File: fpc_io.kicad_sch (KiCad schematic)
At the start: 23 parts, among them J4 SM03B-SRSS-TB, J5 Conn_01x24_Socket, J6 Conn_02x06_Odd_Even, Y2 ABM8G-B4Y-T3

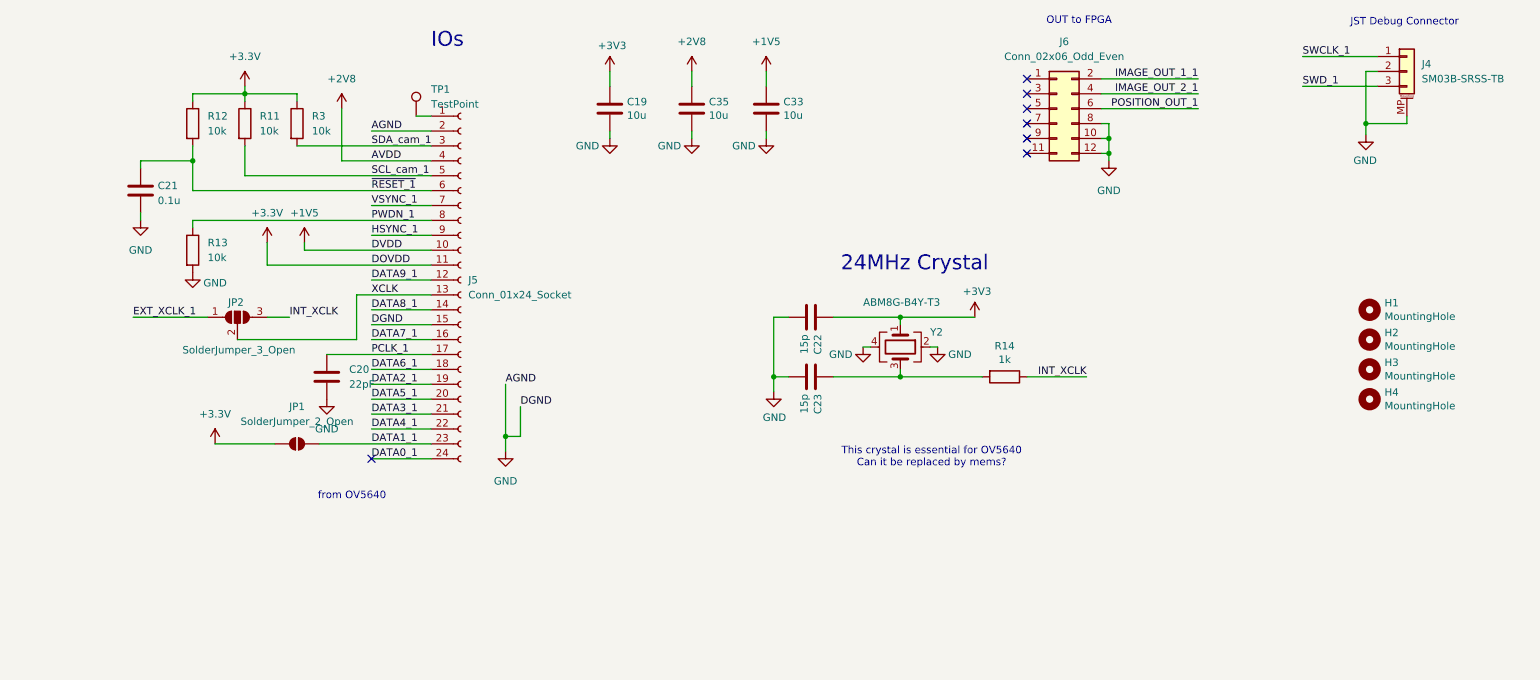
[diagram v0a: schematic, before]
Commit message: discarded 24MHz crystal. ERC passed 1st time
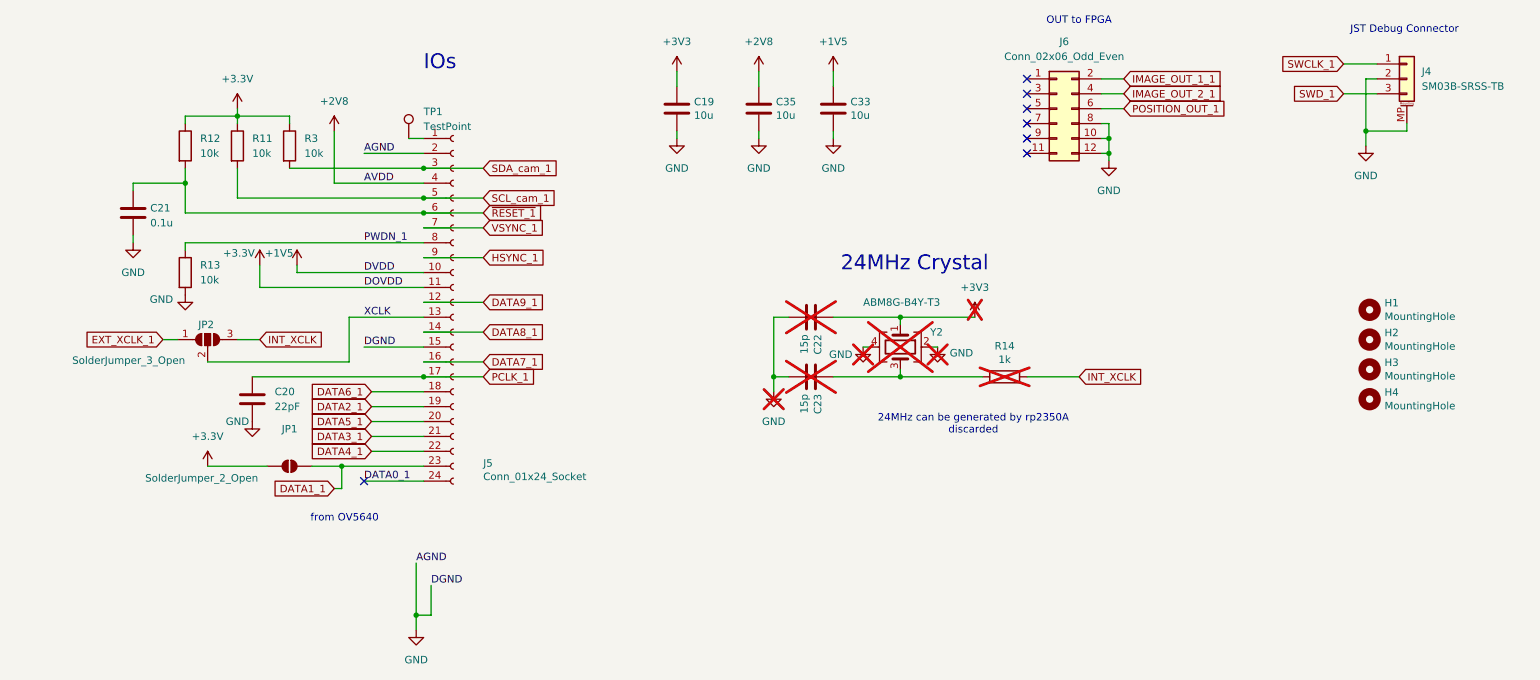
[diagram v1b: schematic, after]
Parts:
- C22, C23, R14, Y2: now not fitted
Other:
- note added: "24MHz can be generated by rp2350A discarded"
- note removed: "This crystal is essential for OV5640 Can it be replaced by mems?"
- moved on the sheet: C19, C20, C21, C33, C35, J4, J5, JP1, JP2, R11, R12, R13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

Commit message: updates in layout
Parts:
- removed JP1: SolderJumper_2_Open, symbol Jumper:SolderJumper_2_Open
- removed JP2: SolderJumper_3_Open, symbol Jumper:SolderJumper_3_Open
- added R10, R24, R9: 0R, Resistor_SMD:R_0603_1608Metric_Pad0.98x0.95mm_HandSolder, symbol Device:R
- TP1: footprint (none) -> TestPoint:TestPoint_Pad_D1.0mm
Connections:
- net +3.3V: now also C19.1, R24.1
- net DATA1_1: now also R24.2
- net EXT_XCLK_1: now also R9.1
- net INT_XCLK: now also R10.2
- net XCLK: now also R10.1, R9.2
- net +3V3: no longer names the net of C22.1, Y2.1
- net +3V3: no longer C19.1

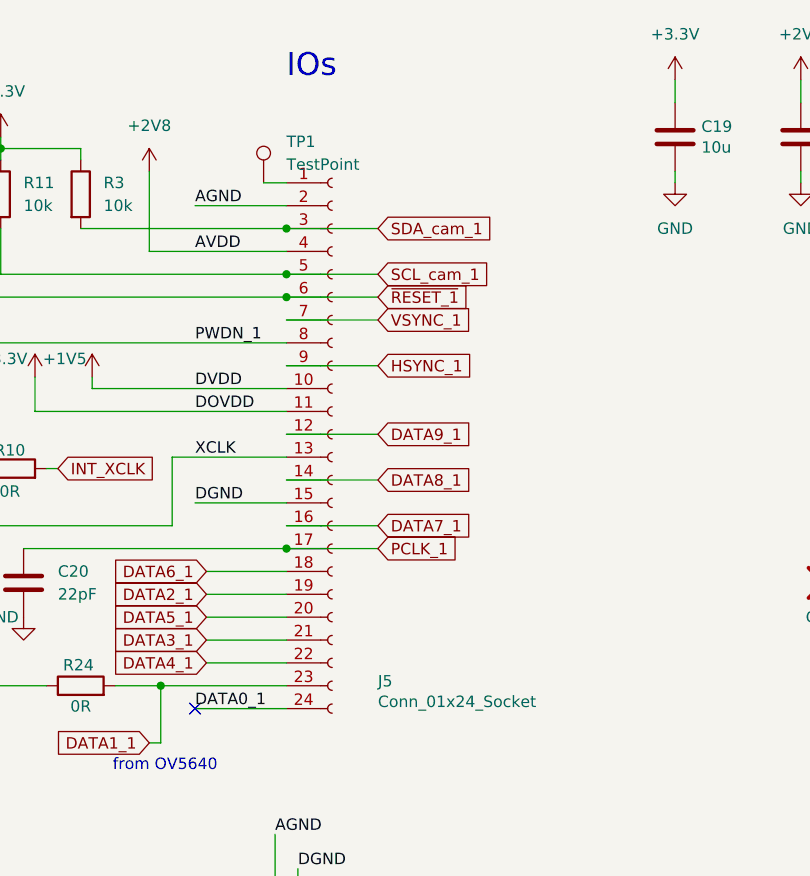
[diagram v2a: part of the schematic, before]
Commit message: vital change to pin order of connector; RP2350 SMPS layout changed
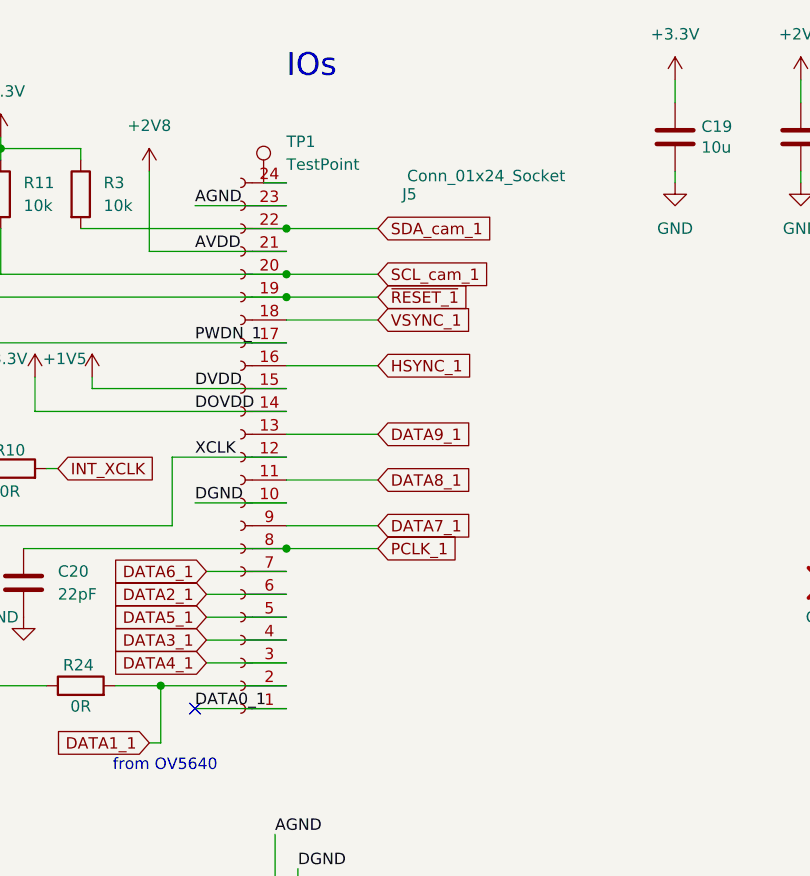
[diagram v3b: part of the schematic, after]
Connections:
- net +1V5: now also J5.15 (Pin_15); no longer J5.10 (Pin_10)
- net +2V8: now also J5.21 (Pin_21); no longer J5.4 (Pin_4)
- net +3.3V: now also J5.14 (Pin_14); no longer J5.11 (Pin_11)
- net DATA0_1: now also J5.1 (Pin_1); no longer J5.24 (Pin_24)
- net DATA1_1: now also J5.2 (Pin_2); no longer J5.23 (Pin_23)
- net DATA2_1: now also J5.6 (Pin_6); no longer J5.19 (Pin_19)
- net DATA3_1: now also J5.4 (Pin_4); no longer J5.21 (Pin_21)
- net DATA4_1: now also J5.3 (Pin_3); no longer J5.22 (Pin_22)
- net DATA5_1: now also J5.5 (Pin_5); no longer J5.20 (Pin_20)
- net DATA6_1: now also J5.7 (Pin_7); no longer J5.18 (Pin_18)
- net DATA7_1: now also J5.9 (Pin_9); no longer J5.16 (Pin_16)
- net DATA8_1: now also J5.11 (Pin_11); no longer J5.14 (Pin_14)
- net DATA9_1: now also J5.13 (Pin_13); no longer J5.12 (Pin_12)
- net GND: now also J5.10 (Pin_10), J5.23 (Pin_23); no longer J5.15 (Pin_15), J5.2 (Pin_2)
- net HSYNC_1: now also J5.16 (Pin_16); no longer J5.9 (Pin_9)
- net PCLK_1: now also J5.8 (Pin_8); no longer J5.17 (Pin_17)
- net PWDN_1: now also J5.17 (Pin_17); no longer J5.8 (Pin_8)
- net SCL_cam_1: now also J5.20 (Pin_20); no longer J5.5 (Pin_5)
- net SDA_cam_1: now also J5.22 (Pin_22); no longer J5.3 (Pin_3)
- net VSYNC_1: now also J5.18 (Pin_18); no longer J5.7 (Pin_7)
- net XCLK: now also J5.12 (Pin_12); no longer J5.13 (Pin_13)
- net ~{RESET_1}: now also J5.19 (Pin_19); no longer J5.6 (Pin_6)
- net at TP1.1: now also J5.24 (Pin_24); no longer J5.1 (Pin_1)
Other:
- moved on the sheet: J5
